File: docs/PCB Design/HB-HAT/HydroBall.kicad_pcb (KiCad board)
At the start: 4 copper layers, 75.9 x 105.9 mm, 64 parts, among them IC1 HIH8130-021-001, J1 Conn_01x05, J11 Conn_02x05_Top_Bottom, J13 Conn_01x06, J14 Conn_02x04_Counter_Clockwise, J2 Conn_01x07, J3 Conn_01x05, J4 Conn_01x05, J5 Conn_01x06, J6 Conn_01x05, J7 Conn_01x05, J8 Raspberry_Pi_2_3, J9 Conn_01x03, Q2 2N7000, U4 INA238AIDGSR, U7 PCA9533DP_02,118, U8 DS3231MZ

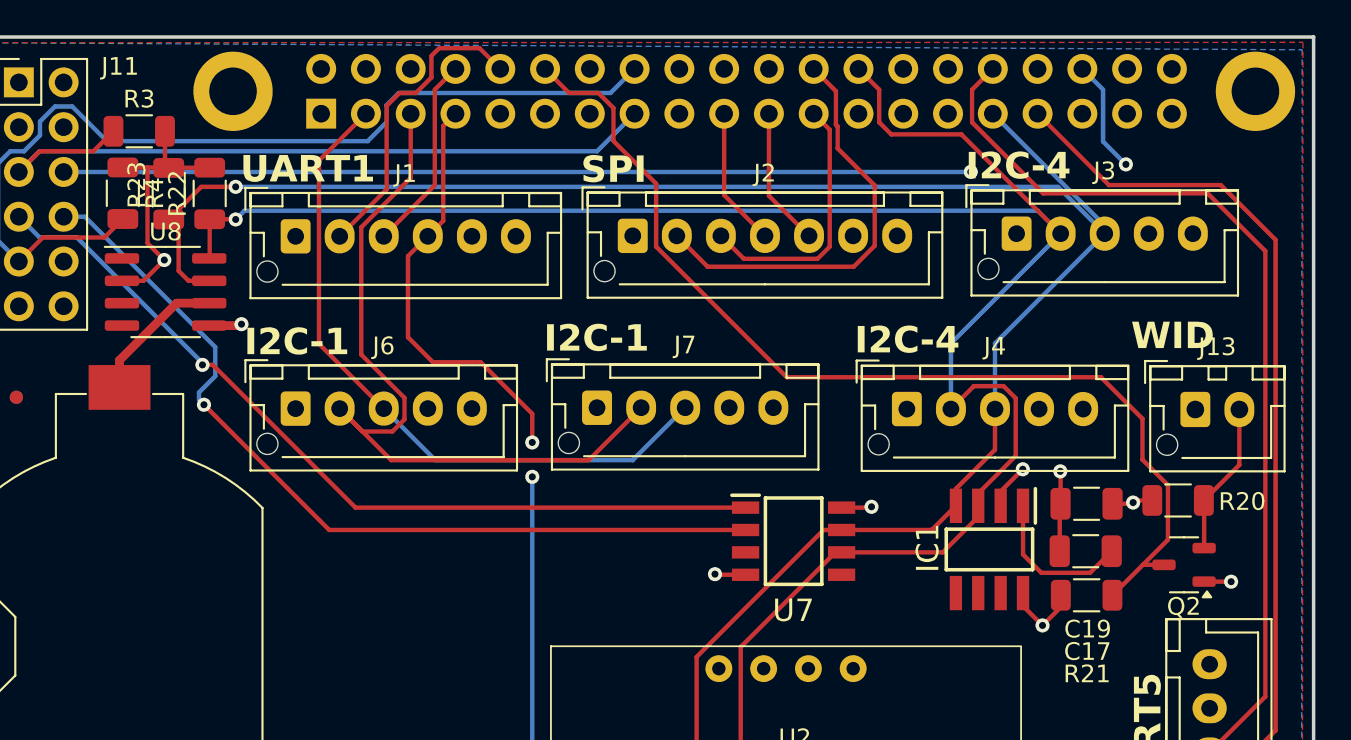
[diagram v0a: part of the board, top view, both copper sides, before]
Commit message: HB-HAT replace led driver by mosfet connected on GPIO
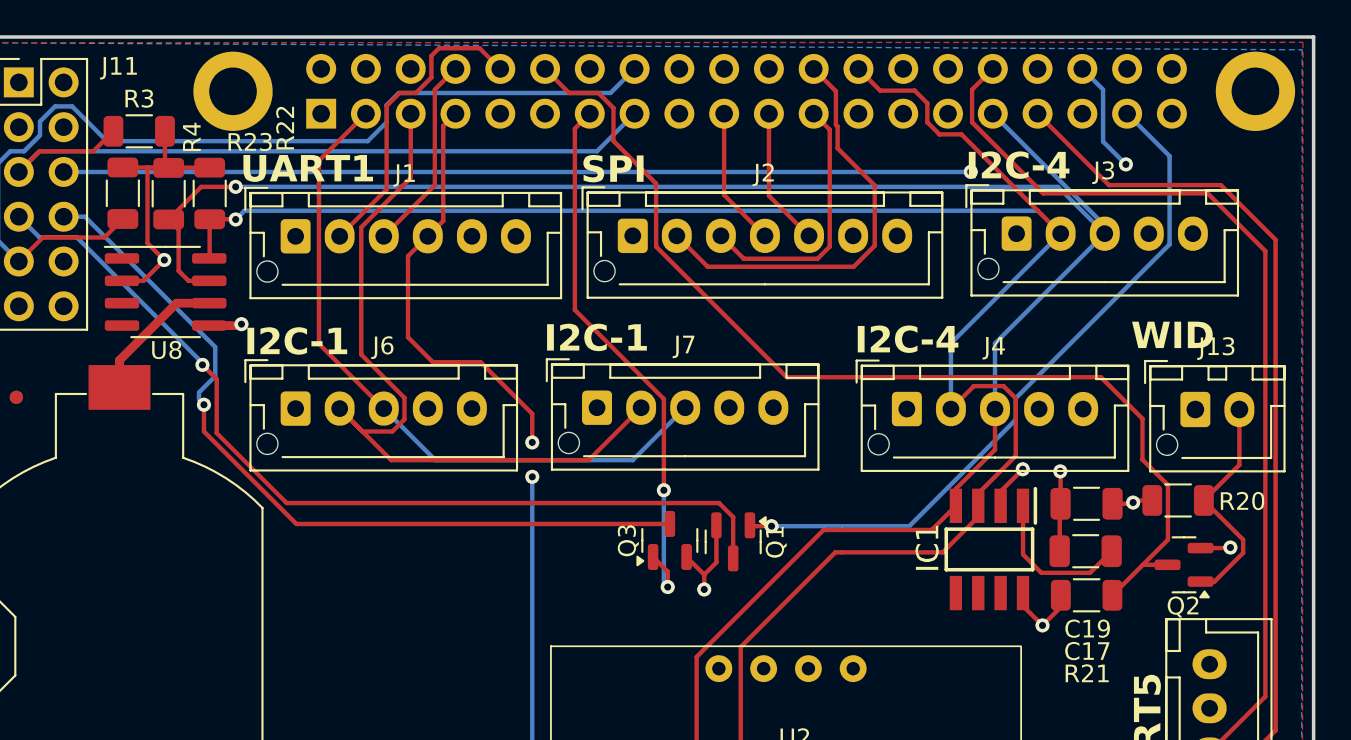
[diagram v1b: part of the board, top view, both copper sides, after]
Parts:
- removed U7: PCA9533DP_02,118, KiCad:SOIC127P600X175-8N
- added Q1: 2N7002, Package_TO_SOT_SMD:SOT-23, F.Cu at (144.6, 69.0)
- added Q3: 2N7002, Package_TO_SOT_SMD:SOT-23, F.Cu at (141.0, 69.0)
- Q2: value 2N7000 -> 2N7002; footprint Package_TO_SOT_SMD:SOT-23-3 -> Package_TO_SOT_SMD:SOT-23
- turned R4 to 90 degrees
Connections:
- J8 pad 13: unconnected-(J8-GPIO27-Pad13) -> Green-g
- J8 pad 37: unconnected-(J8-GPIO26-Pad37) -> Red_g
- Q2 pad 1: GND -> Net-(J13-Pin_2)
- Q2 pad 2: Net-(J13-Pin_2) -> GND
- R4 pad 1: +3.3V -> Pwr_Pulse
- R4 pad 2: Pwr_Pulse -> +3.3V
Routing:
- net Red_g: track 0.00 -> 39.6 mm, vias 0 -> 1
- net Green-g: track 0.00 -> 31.4 mm, vias 0 -> 2
- net Net-(J13-Pin_2): track 8.70 -> 13.0 mm
- net Red: track 48.1 -> 51.8 mm
- net Green: track 49.1 -> 45.5 mm
- net GND: track 125.8 -> 129.1 mm
- net +3.3V: track 46.8 -> 45.1 mm, vias 6 -> 5
- net SCK4: track 179.8 -> 178.7 mm

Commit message: PCB : HB-HAT replace led driver by mosfet connected on gpio
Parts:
- Q1, Q2, Q3: value 2N7002 -> 2N7000
- moved J9 2.43 mm to (107.3, 122.1)
- moved Q1 0.15 mm to (144.5, 69.2)
- moved Q3 0.09 mm to (141.1, 69.0)
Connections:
- Q1 pad 1: Red_g -> Red
- Q1 pad 3: Red -> Red_g
- Q3 pad 1: Green-g -> Green
- Q3 pad 3: Green -> Green-g
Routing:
- net Net-(J9-Pin_3): track 11.4 -> 13.8 mm
- net Red_g: track 39.6 -> 41.5 mm
- net Green-g: track 31.4 -> 33.0 mm
- net Red: track 51.8 -> 50.6 mm

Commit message: DC to DC converter replacement with filtration and voltage correction TBC.
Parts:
- C10: value 1nf/2kv -> 4.7nf/2kv
- C13: value 100uf/16v -> DNP
- C5: value 330uf/50v -> 150uf/50v
- C7: value 4.7uf/50v -> DNP
- C8: value 4.7uf/50v -> 10uf/50v
- C9: value 330uf/50v -> 47uf/50v
- L1: value 2.2uH/4A -> 22uH/4A
- PS1: value PDQE20-Q24-S5-D -> REC20K-2405SZ
- R15: value 100r -> 0R
- R16: value 3.57k -> DNP
- R17: value 1.5K -> 169K
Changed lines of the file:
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@@
 			)
 		)
-		(property "Value" "100r"
+		(property "Value" "0R"
 			(at 0 1.82 0)
 			(layer "F.Fab")
@@
 			)
 		)
-		(property "Value" "1nf/2kv"
+		(property "Value" "4.7nf/2kv"
 			(at 0 1.85 -90)
 			(layer "F.Fab")
@@
 			)
 		)
-		(property "Value" "100uf/16v"
+		(property "Value" "DNP"
 			(at 0 4.35 90)
 			(layer "F.Fab")
@@
 			)
 		)
-		(property "Value" "4.7uf/50v"
+		(property "Value" "DNP"
 			(at -9.875 -8.975 90)
 			(layer "F.Fab")
@@
 			)
 		)
-		(property "Value" "3.57k"
+		(property "Value" "DNP"
 			(at 0 1.82 90)
 			(layer "F.Fab")
@@
 			)
 		)
-		(property "Value" "4.7uf/50v"
+		(property "Value" "10uf/50v"
 			(at 0 1.85 90)
 			(layer "F.Fab")
@@
 			)
 		)
-		(property "Value" "2.2uH/4A"
+		(property "Value" "22uH/4A"
 			(at 0 2.28 90)
 			(layer "F.Fab")
@@
 			)
 		)
-		(property "Value" "1.5K"
+		(property "Value" "169K"
 			(at 0 1.82 90)
 			(layer "F.Fab")
@@
 			)
 		)
-		(property "Value" "330uf/50v"
+		(property "Value" "150uf/50v"
 			(at 2.5 -6.25 90)
 			(layer "B.Fab")
@@
 			)
 		)
-		(property "Value" "PDQE20-Q24-S5-D"
+		(property "Value" "REC20K-2405SZ"
 			(at 0.635 -13.97 0)
 			(layer "B.Fab")
@@
 			)
 		)
-		(property "Value" "330uf/50v"
+		(property "Value" "47uf/50v"
 			(at 2.5 -6.25 90)
 			(layer "B.Fab")

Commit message: PCB HB-HAT : fix mosfet pinout
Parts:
- Q1, Q2, Q3: value 2N7000 -> 2N7002
- moved Q2 25.7 mm to (144.5, 69.0), turned to 90 degrees
- moved Q1 25.6 mm to (170.1, 70.3), turned to 180 degrees
- moved Q3 0.49 mm to (140.6, 69.0)
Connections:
- Q1 pad 1: Red -> Net-(J13-Pin_2)
- Q1 pad 3: Red_g -> W_Intrusion
- Q2 pad 1: Net-(J13-Pin_2) -> Red
- Q2 pad 3: W_Intrusion -> Red_g
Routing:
- net Red_g: track 41.5 -> 40.8 mm
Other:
- board text added: "PN: HB-HAT Rev.06 27022025DD"
- board text removed: "PN: HB-HAT Rev.05 10022025DD"
